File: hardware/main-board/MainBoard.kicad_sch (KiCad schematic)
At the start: 15 parts, among them J1 Conn_01x03_Pin, J2 Conn_01x03_Pin, J3 Conn_01x03_Pin, J4 Conn_01x03_Pin, SW1 SW_SP3T, SW2 SW_SP3T, U1 CD22M3494MQZ, U2 TL081, U3 TL071, U4 TL071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

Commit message: I think Parker would look good if he got shot in the head
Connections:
- net Cell_0_Buff: now also U1.15 (Y5); no longer U1.35 (Y1)
- net Cell_1_Buff: now also U1.13 (Y6); no longer U1.37 (Y2)
- net Cell_2_Buff: now also U1.10 (Y7); no longer U1.39 (Y3)
- net Cell_3_Buff: now also U1.39 (Y3); no longer U1.17 (Y4)
- net Signal_In: now also U1.17 (Y4); no longer U1.32 (Y0)
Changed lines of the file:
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@@
+	)
+	(no_connect
+		(at 43.18 26.67)
+	)
+	(no_connect
+		(at 43.18 31.75)
+	)
+	(no_connect
+		(at 43.18 29.21)
 	)
 	(no_connect
@@
 	)
 	(no_connect
-		(at 43.18 39.37)
-	)
-	(no_connect
 		(at 254 49.53)
 	)
@@
 		(at 254 76.2)
 	)
-	(no_connect
-		(at 43.18 41.91)
-	)
-	(no_connect
-		(at 43.18 44.45)
-	)
 	(wire
 		(pts
@@
 	)
 	(label "Cell_2_Buff"
-		(at 43.18 34.29 180)
+		(at 43.18 44.45 180)
 		(effects
 			(font
@@
 	)
 	(label "Cell_1_Buff"
-		(at 43.18 31.75 180)
+		(at 43.18 41.91 180)
 		(effects
 			(font
@@
 	)
 	(label "Cell_3_Buff"
-		(at 43.18 36.83 180)
+		(at 43.18 34.29 180)
 		(effects
 			(font
@@
 	)
 	(label "Cell_0_Buff"
-		(at 43.18 29.21 180)
+		(at 43.18 39.37 180)
 		(effects
 			(font
@@
 	)
 	(label "Signal_In"
-		(at 43.18 26.67 180)
-		(effects
-			(font
+		(at 43.18 36.83 180)
+		(effects
+			(font

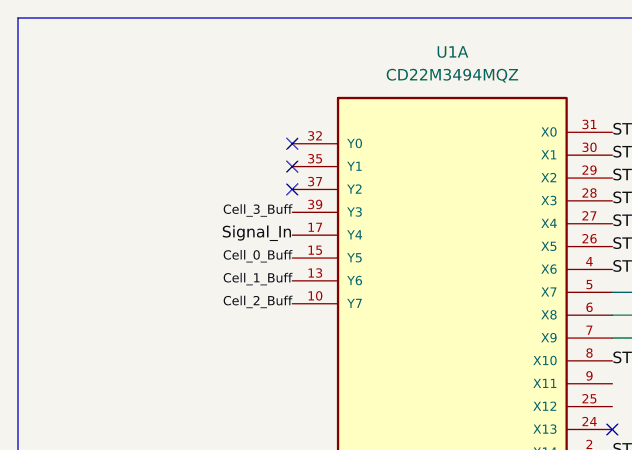
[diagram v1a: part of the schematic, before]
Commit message: feat: Schematic changes for top level +/-5V
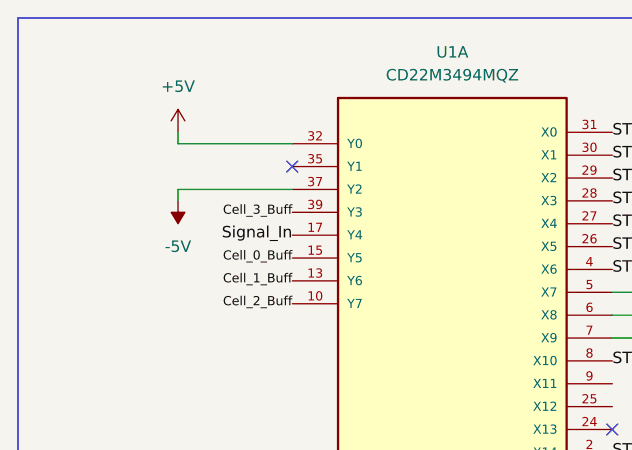
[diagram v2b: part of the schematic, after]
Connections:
- net +5V: now also U1.32 (Y0)
- net -5V: now also U1.37 (Y2)
- no-connect marks 14 -> 12
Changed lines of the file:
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@@
 	)
 	(no_connect
-		(at 43.18 26.67)
-	)
-	(no_connect
-		(at 43.18 31.75)
-	)
-	(no_connect
 		(at 43.18 29.21)
 	)
@@
 	(wire
 		(pts
+			(xy 30.48 25.4) (xy 30.48 26.67)
+		)
+		(stroke
+			(width 0)
+			(type default)
+		)
+	)
+	(wire
+		(pts
 			(xy 96.52 29.21) (xy 97.79 29.21)
 		)
@@
 	(wire
 		(pts
+			(xy 30.48 26.67) (xy 43.18 26.67)
+		)
+		(stroke
+			(width 0)
+			(type default)
+		)
+	)
+	(wire
+		(pts
 			(xy 96.52 60.96) (xy 97.79 60.96)
 		)
@@
 	(wire
 		(pts
+			(xy 30.48 31.75) (xy 43.18 31.75)
+		)
+		(stroke
+			(width 0)
+			(type default)
+		)
+	)
+	(wire
+		(pts
 			(xy 147.32 29.21) (xy 148.59 29.21)
 		)
@@
 	(wire
 		(pts
+			(xy 30.48 33.02) (xy 30.48 31.75)
+		)
+		(stroke
+			(width 0)
+			(type default)
+		)
+	)
+	(wire
+		(pts
 			(xy 147.32 25.4) (xy 148.59 25.4)
 		)
@@
 	)
 	(symbol
+		(lib_id "power:+5V")
+		(at 30.48 25.4 0)
+		(unit 1)
+		(exclude_from_sim no)
+		(in_bom yes)
+		(on_board yes)
+		(dnp no)
+		(fields_autoplaced yes)
+		(property "Reference" "#PWR025"
+			(at 30.48 29.21 0)
+			(effects
+				(font
+					(size 1.27 1.27)
+				)
+				(hide yes)
+			)
+		)
+		(property "Value" "+5V"
+			(at 30.48 20.32 0)
+			(effects
+				(font
+					(size 1.27 1.27)
+				)
+			)
+		)
+		(property "Footprint" ""
+			(at 30.48 25.4 0)
+			(effects
+				(font
+					(size 1.27 1.27)
+				)
+				(hide yes)
+			)
+		)
+		(property "Datasheet" ""
+			(at 30.48 25.4 0)
+			(effects
+				(font
+					(size 1.27 1.27)
+				)
+				(hide yes)
+			)
+		)
+		(property "Description" "Power symbol creates a global label with name \"+5V\""
+			(at 30.48 25.4 0)
+			(effects
+				(font
+					(size 1.27 1.27)
+				)
+				(hide yes)
+			)
+		)
+		(pin "1"
+		)
+		(instances
+			(project ""
+				(path "/5dd933ff-bc57-4741-8957-85d8c6e75130"
+					(reference "#PWR025")
+					(unit 1)
+				)
+			)
+		)
+	)
+	(symbol
 		(lib_id "Connector:Conn_01x03_Pin")
 		(at 81.28 156.21 180)
@@
 					(unit 1)
 				)
+			)
+		)
+	)
+	(symbol
+		(lib_id "power:-5V")
+		(at 30.48 33.02 180)
+		(unit 1)
+		(exclude_from_sim no)
+		(in_bom yes)
+		(on_board yes)
+		(dnp no)
+		(fields_autoplaced yes)
+		(property "Reference" "#PWR020"
+			(at 30.48 29.21 0)
+			(effects
+				(font
+					(size 1.27 1.27)
+				)
+				(hide yes)
+			)
+		)
+		(property "Value" "-5V"
+			(at 30.48 38.1 0)
+			(effects
+				(font
+					(size 1.27 1.27)
+				)
+			)
+		)
+		(property "Footprint" ""
+			(at 30.48 33.02 0)
+			(effects
+				(font
+					(size 1.27 1.27)
+				)
+				(hide yes)
+			)
+		)
+		(property "Datasheet" ""
+			(at 30.48 33.02 0)
+			(effects
+				(font
+					(size 1.27 1.27)
+				)
+				(hide yes)
+			)
+		)
+		(property "Description" "Power symbol creates a global label with name \"-5V\""
+			(at 30.48 33.02 0)
+			(effects
+				(font
+					(size 1.27 1.27)
+				)
+				(hide yes)
+			)
+		)
+		(pin "1"
+		)
+		(instances
+			(project ""
+				(path "/5dd933ff-bc57-4741-8957-85d8c6e75130"
+					(reference "#PWR020")
+					(unit 1)
+				)

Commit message: feat: Routing for top level +/- 5V
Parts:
- SW1, SW2: footprint Button_Switch_SMD:SW_DIP_SPSTx02_Slide_6.7x6.64mm_W6.73mm_P2.54mm_LowProfile_JPin -> Button_Switch_THT:SW_Slide_SP3T_Straight_CK_OS103012MU1QP1
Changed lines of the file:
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@@
 			)
 		)
-		(property "Footprint" "Button_Switch_SMD:SW_DIP_SPSTx02_Slide_6.7x6.64mm_W6.73mm_P2.54mm_LowProfile_JPin"
+		(property "Footprint" "Button_Switch_THT:SW_Slide_SP3T_Straight_CK_OS103012MU1QP1"
 			(at 34.925 151.765 0)
 			(effects
@@
 			)
 		)
-		(property "Footprint" "Button_Switch_SMD:SW_DIP_SPSTx02_Slide_6.7x6.64mm_W6.73mm_P2.54mm_LowProfile_JPin"
+		(property "Footprint" "Button_Switch_THT:SW_Slide_SP3T_Straight_CK_OS103012MU1QP1"
 			(at 98.425 102.235 0)
 			(effects

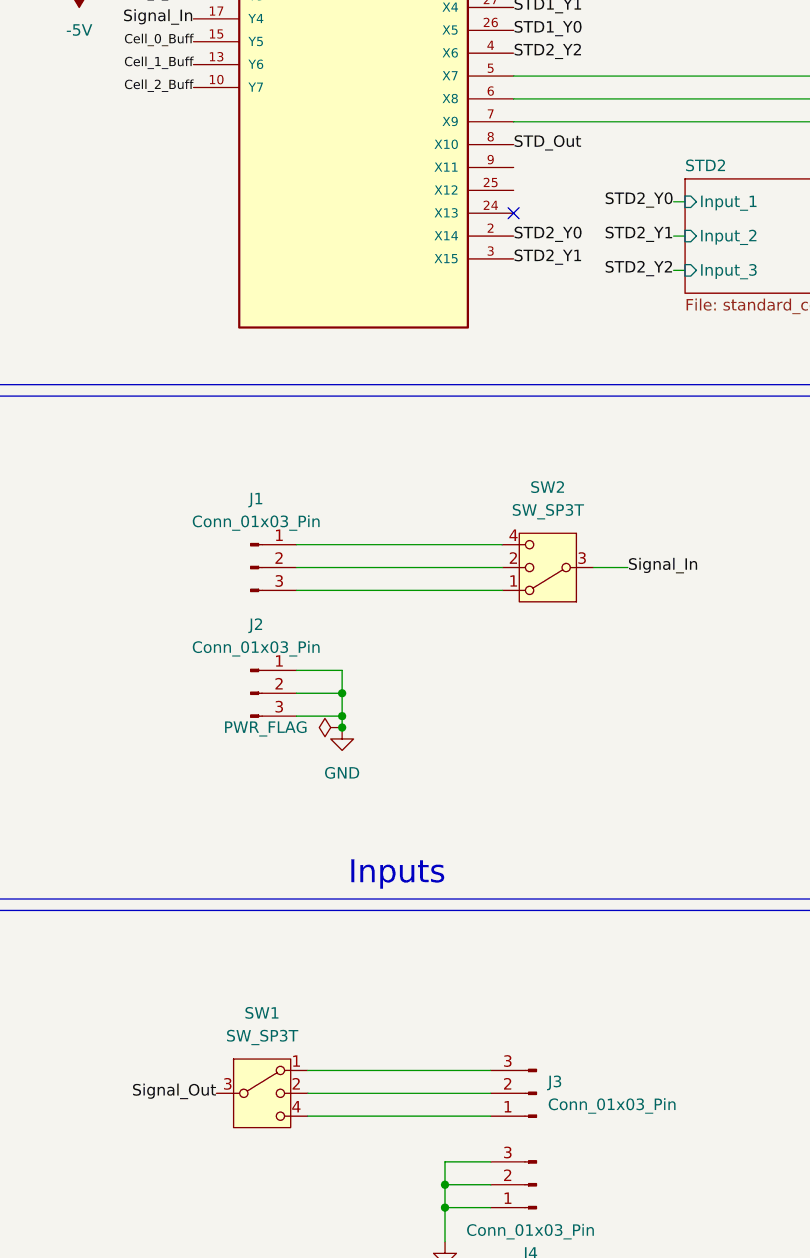
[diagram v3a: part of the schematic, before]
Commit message: feat: ERC + DRC fixes
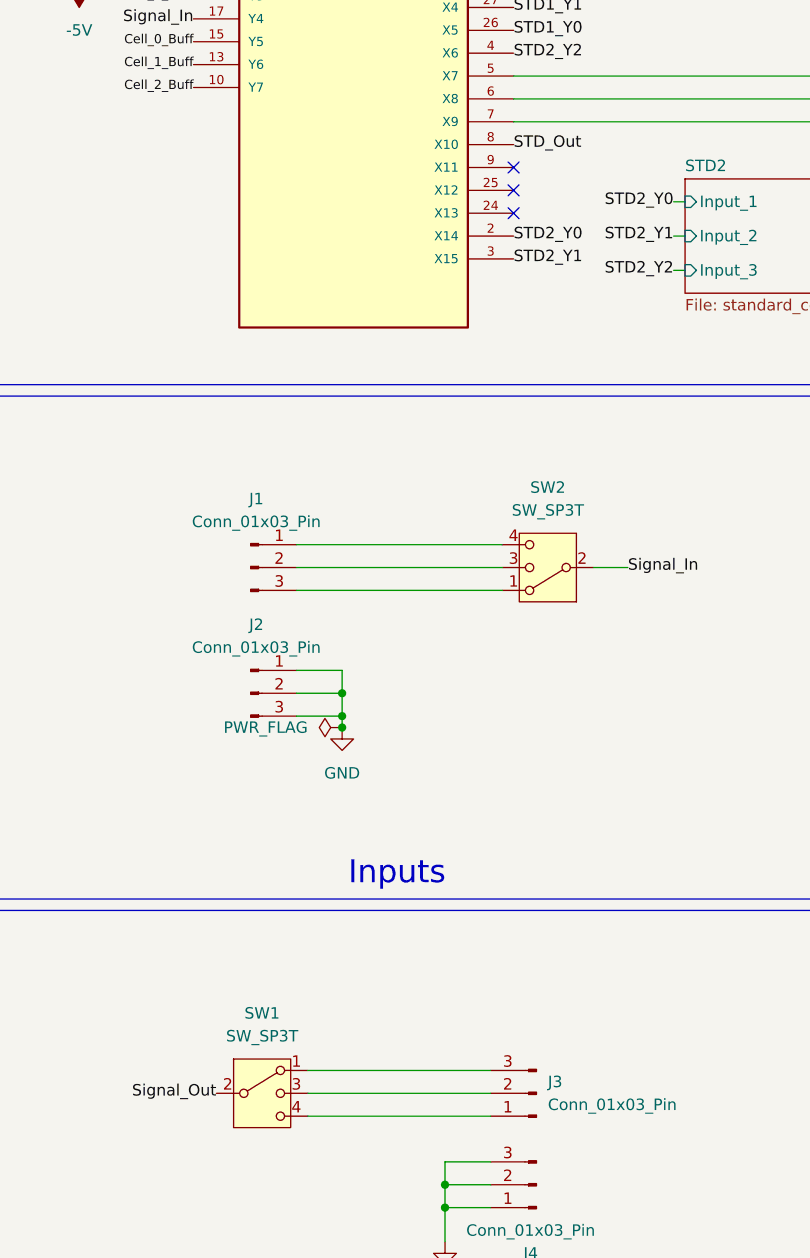
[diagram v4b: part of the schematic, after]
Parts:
- SW1, SW2: symbol Switch:SW_SP3T -> SeniorDesign:SW_SP3T_2P
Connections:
- net Signal_In: now also SW2.2; no longer SW2.3
- net Signal_Out: now also SW1.2; no longer SW1.3
- net at J1.2 (Pin_2): now also SW2.3; no longer SW2.2
- net at J3.2 (Pin_2): now also SW1.3; no longer SW1.2
- no-connect marks 12 -> 14
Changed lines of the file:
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@@
 	)
 	(no_connect
+		(at 78.74 55.88)
+	)
+	(no_connect
 		(at 254 49.53)
 	)
@@
 	)
 	(no_connect
+		(at 78.74 53.34)
+	)
+	(no_connect
 		(at 251.46 49.53)
 	)
@@
 	)
 	(symbol
-		(lib_id "Switch:SW_SP3T")
+		(lib_id "SeniorDesign:SW_SP3T_2P")
 		(at 50.8 156.21 0)
 		(unit 1)
@@
 	)
 	(symbol
-		(lib_id "Switch:SW_SP3T")
+		(lib_id "SeniorDesign:SW_SP3T_2P")
 		(at 82.55 97.79 180)
 		(unit 1)

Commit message: feat: Part nos plus some micro fixup
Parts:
- SW1, SW2: DKPN (none) -> OS103011MS8QP1
- U1: MPN (none) -> 968-CD22M3494MQZ
- U3, U4, U5, U6: DKPN (none) -> TL071HIDR
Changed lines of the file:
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@@
+			)
+		)
+		(property "DKPN" "TL071HIDR"
+			(at 251.46 41.91 0)
+			(effects
+				(font
+					(size 1.27 1.27)
+				)
+				(hide yes)
 			)
 		)
@@
 			)
 		)
+		(property "DKPN" "TL071HIDR"
+			(at 251.46 68.58 0)
+			(effects
+				(font
+					(size 1.27 1.27)
+				)
+				(hide yes)
+			)
+		)
 		(pin "2"
 		)
@@
 			)
 		)
+		(property "DKPN" "TL071HIDR"
+			(at 251.46 121.92 0)
+			(effects
+				(font
+					(size 1.27 1.27)
+				)
+				(hide yes)
+			)
+		)
 		(pin "2"
 		)
@@
 			)
 		)
+		(property "DKPN" "OS103011MS8QP1"
+			(at 50.8 156.21 0)
+			(effects
+				(font
+					(size 1.27 1.27)
+				)
+				(hide yes)
+			)
+		)
 		(pin "4"
 		)
@@
 			)
 		)
+		(property "DKPN" "TL071HIDR"
+			(at 251.46 95.25 0)
+			(effects
+				(font
+					(size 1.27 1.27)
+				)
+				(hide yes)
+			)
+		)
 		(pin "2"
 		)
@@
 			)
 		)
+		(property "MPN" "968-CD22M3494MQZ"
+			(at 60.96 62.23 0)
+			(effects
+				(font
+					(size 1.27 1.27)
+				)
+				(hide yes)
+			)
+		)
 		(pin "30"
 		)
@@
 			(at 82.55 97.79 0)
 			(effects
+				(font
+					(size 1.27 1.27)
+				)
+				(hide yes)
+			)
+		)
+		(property "DKPN" "OS103011MS8QP1"
+			(at 82.55 97.79 0)
+			(effects

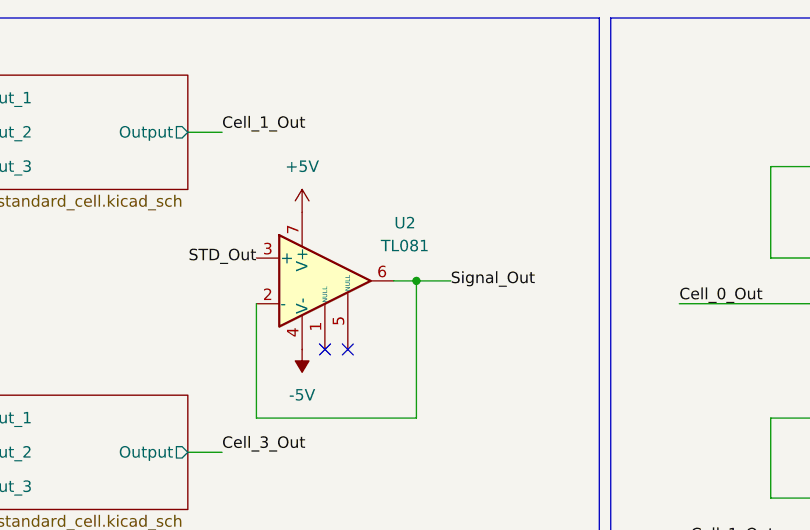
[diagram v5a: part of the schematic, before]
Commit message: finalized component list, fixed DRC errors
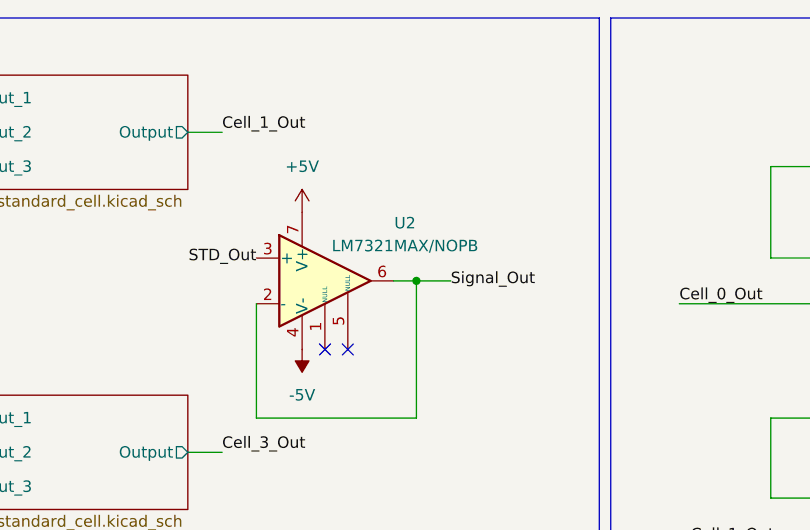
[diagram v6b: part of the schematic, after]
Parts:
- F1, F2, F3: DKPN (none) -> C2Q500
- U1: DKPN (none) -> CD22M3494MQZ
- U2: value TL081 -> LM7321MAX/NOPB; DKPN (none) -> LM7321MAX/NOPB
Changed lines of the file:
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@@
+			)
+		)
+		(property "DKPN" "C2Q500"
+			(at 212.09 132.08 0)
+			(effects
+				(font
+					(size 1.27 1.27)
+				)
+				(hide yes)
 			)
 		)
@@
 			)
 		)
+		(property "DKPN" "CD22M3494MQZ"
+			(at 60.96 62.23 0)
+			(effects
+				(font
+					(size 1.27 1.27)
+				)
+				(hide yes)
+			)
+		)
 		(pin "30"
 		)
@@
 			)
 		)
-		(property "Value" "TL081"
+		(property "Value" "LM7321MAX/NOPB"
 			(at 198.12 38.0298 0)
 			(effects
@@
 			)
 		)
-		(property "Datasheet" "http://www.ti.com/lit/ds/symlink/tl081.pdf"
+		(property "Datasheet" "https://www.ti.com/lit/ds/symlink/lm7321.pdf?HQS=dis-dk-null-digikeymode-dsf-pf-null-wwe&ts=1774276721362&ref_url=https%253A%252F%252Fwww.ti.com%252Fgeneral%252Fdocs%252Fsuppproductinfo.tsp%253FdistId%253D10%2526gotoUrl%253Dhttps%253A%252F%252Fwww.ti.com%252Flit%252Fgpn%252Flm7321"
 			(at 193.04 38.1 0)
 			(effects
@@
 			)
 		)
-		(property "Description" "Single JFET-Input Operational Amplifiers, DIP-8/SOIC-8"
+		(property "Description" ""
+			(at 189.23 41.91 0)
+			(effects
+				(font
+					(size 1.27 1.27)
+				)
+				(hide yes)
+			)
+		)
+		(property "DKPN" "LM7321MAX/NOPB"
 			(at 189.23 41.91 0)
 			(effects
@@
 			)
 		)
+		(property "DKPN" "C2Q500"
+			(at 214.63 114.3 0)
+			(effects
+				(font
+					(size 1.27 1.27)
+				)
+				(hide yes)
+			)
+		)
 		(pin "1"
 		)
@@
 			(at 208.28 107.95 0)
 			(effects
+				(font
+					(size 1.27 1.27)
+				)
+				(hide yes)
+			)
+		)
+		(property "DKPN" "C2Q500"
+			(at 208.28 107.95 0)
+			(effects
